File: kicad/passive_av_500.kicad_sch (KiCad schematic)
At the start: 22 parts, among them J1 Raspberry_Pi_5, J2 Conn_Coaxial, J3 Conn_01x05, J4 AudioJack4

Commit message: Add "tooling holes" and reconnect J1 pin 39 to improve GND plane
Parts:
- added H1, H2: MountingHole, MountingHole:ToolingHole_1.152mm, symbol Mechanical:MountingHole
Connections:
- net GND: now also J1.39 (GND)
- no-connect marks 22 -> 21
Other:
- note added: "Not connecting GND pin 6, to reduce the risk of accidentally shorting 5V if wrongly installed."
- note removed: "Not connecting GND pins 6 and 39, to reduce the risk of accidentally shorting 5V or 3.3V if wrongly installed."
- moved on the sheet: J2

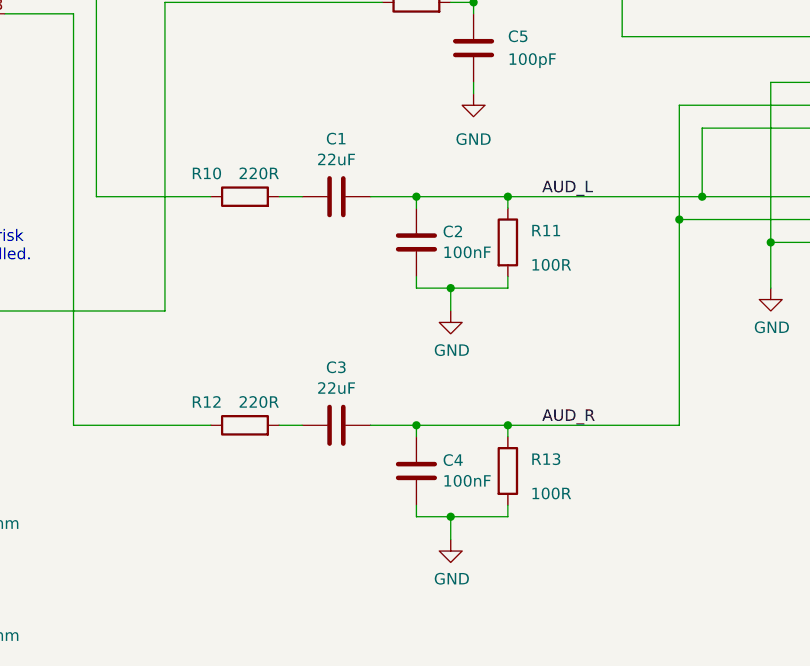
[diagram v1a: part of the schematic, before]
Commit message: Candidate "rev 2.1" version
Increase R10,R12 and R11,R13 to 300R and 120R. This will slightly
reduce audio level, but ensures peak GPIO current is below 12mA
and total can't exceed 50mA (even if all A/V outputs are shorted).

Update README.md, images and production files.
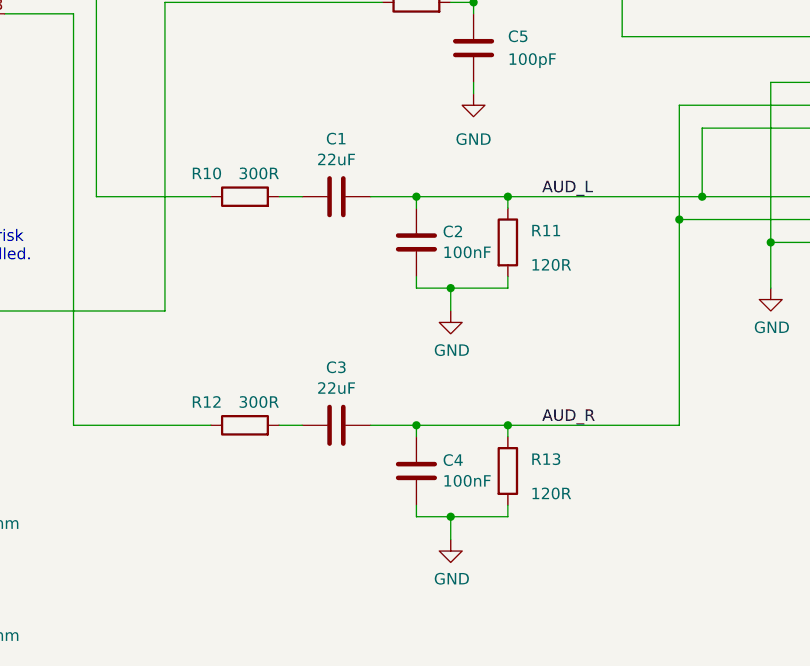
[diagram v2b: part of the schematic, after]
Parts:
- R10, R12: value 220R -> 300R; LCSC C17557 -> C17617
- R11, R13: value 100R -> 120R; LCSC C17408 -> C17437
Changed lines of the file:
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@@
 	(title_block
 		(title "Passive A/V out example circuit for Raspberry Pi 5 series")
-		(date "2025-10-25")
-		(rev "2")
+		(date "2025-11-08")
+		(rev "2.1")
 	)
 	(text "Not connecting GND pin 6, to reduce the risk\nof accidentally shorting 5V if wrongly installed."
@@
 			)
 		)
-		(property "Value" "220R"
+		(property "Value" "300R"
 			(at 128.27 104.14 90)
 			(effects
@@
 			)
 		)
-		(property "LCSC" "C17557"
+		(property "LCSC" "C17617"
 			(at 124.46 106.68 90)
 			(effects
@@
 			)
 		)
-		(property "Value" "100R"
+		(property "Value" "120R"
 			(at 156.21 114.3 0)
 			(effects
@@
 			)
 		)
-		(property "LCSC" "C17408"
+		(property "LCSC" "C17437"
 			(at 153.67 111.76 0)
 			(effects
@@
 			)
 		)
-		(property "Value" "100R"
+		(property "Value" "120R"
 			(at 156.21 139.7 0)
 			(effects
@@
 			)
 		)
-		(property "LCSC" "C17408"
+		(property "LCSC" "C17437"
 			(at 153.67 137.16 0)
 			(effects
@@
 			)
 		)
-		(property "Value" "220R"
+		(property "Value" "300R"
 			(at 128.27 129.54 90)
 			(effects
@@
 			)
 		)
-		(property "LCSC" "C17557"
+		(property "LCSC" "C17617"
 			(at 124.46 132.08 90)
 			(effects
